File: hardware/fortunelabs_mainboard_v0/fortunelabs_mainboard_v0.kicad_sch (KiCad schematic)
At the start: 21 parts, among them J1 Conn_01x04_Pin, J4 Conn_02x08_Odd_Even, U1 ADS1115, U2 MCP23017_ML, U3 ESP32-S3-WROOM-2

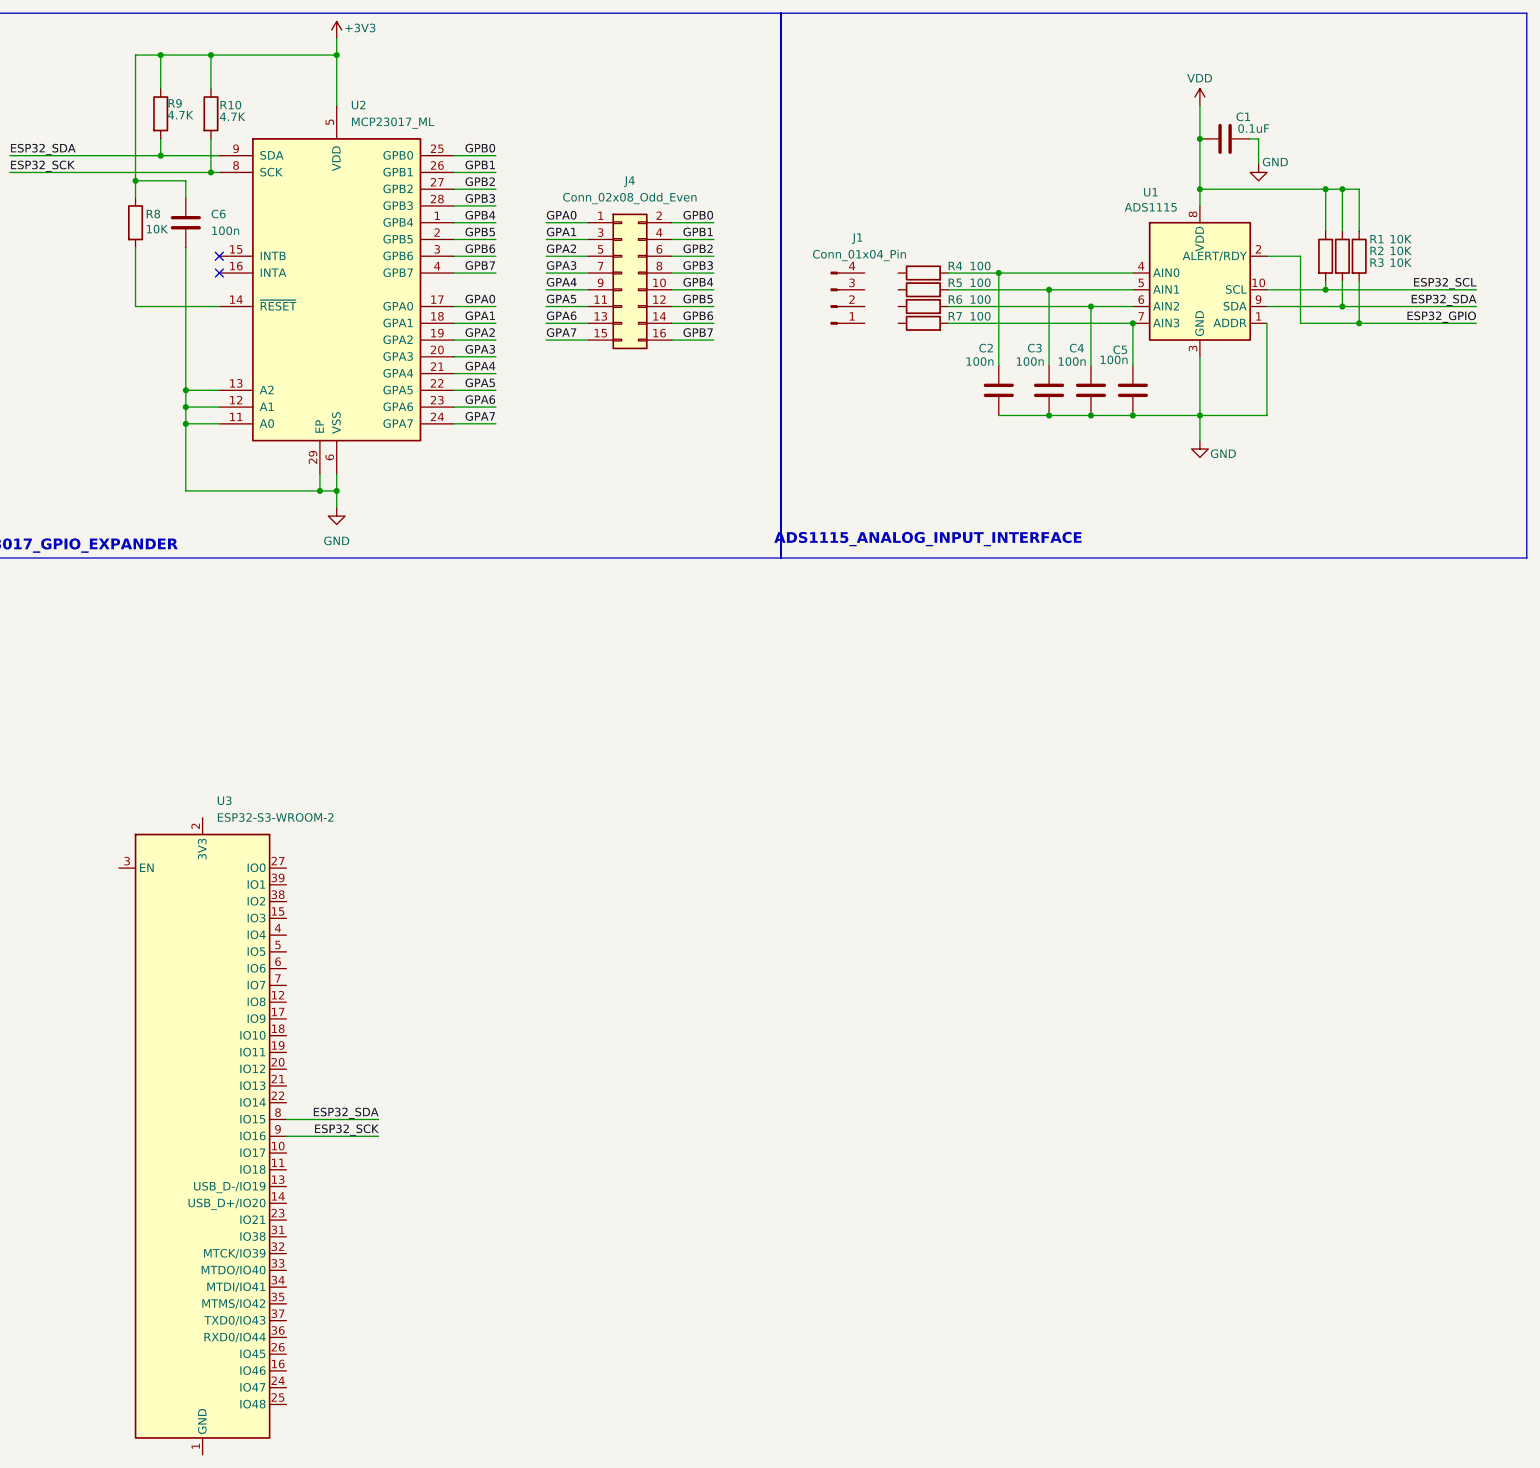
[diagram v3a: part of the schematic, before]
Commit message: refactor: changing pin to Conn_02x04_Odd_Even and restructure ground location
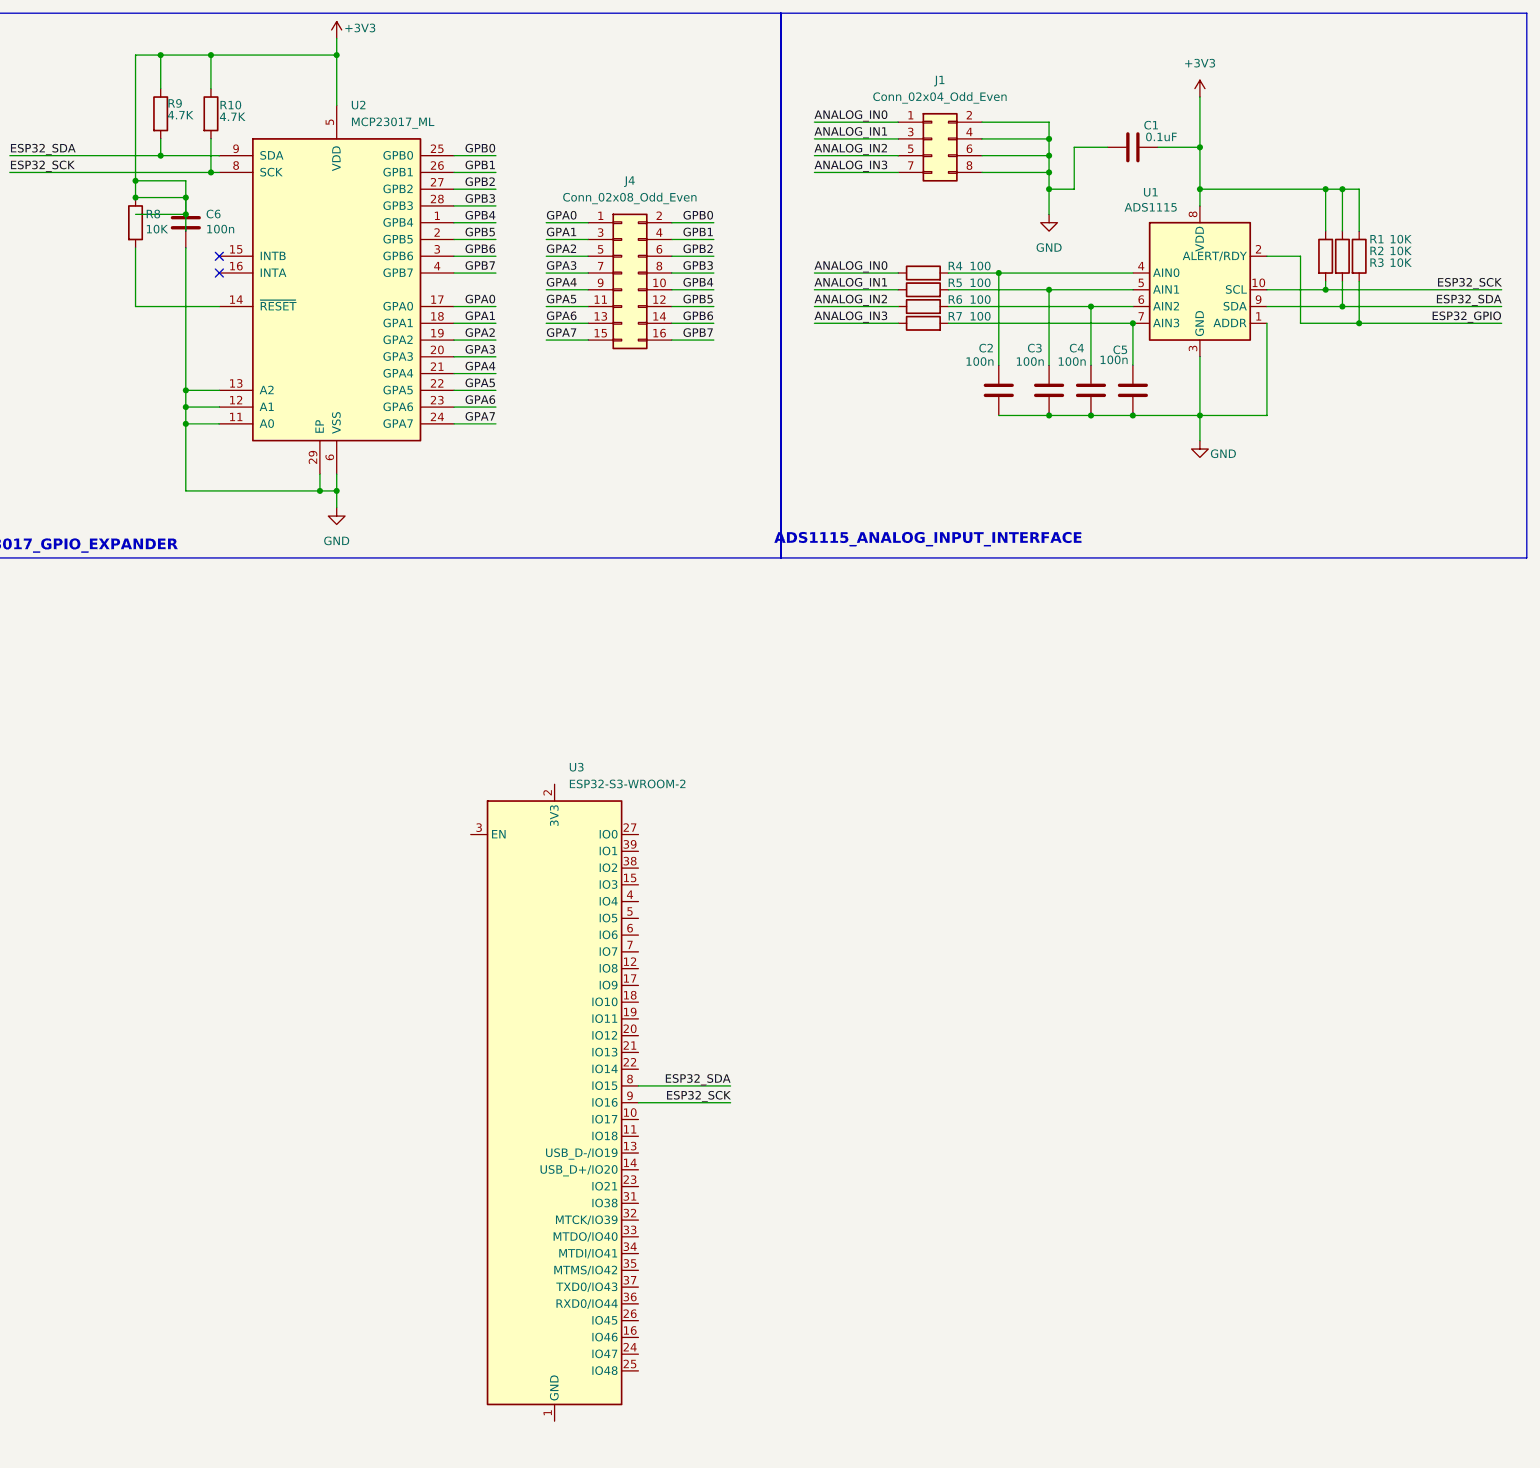
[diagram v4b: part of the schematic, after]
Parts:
- removed J1: Conn_01x04_Pin, symbol Connector:Conn_01x04_Pin
- added J1: Conn_02x04_Odd_Even, symbol Connector_Generic:Conn_02x04_Odd_Even
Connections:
- net ESP32_SCL is gone; now on net ESP32_SCK: R3.2, U1.10 (SCL)
- net +3V3: now also C1.1, R1.1, R2.1, R3.1, U1.8 (VDD)
- net GND: now also C1.2, J1.2 (Pin_2), J1.4 (Pin_4), J1.6 (Pin_6), J1.8 (Pin_8); no longer C1.1
- net ANALOG_IN2: now reaches R6.1
- net ANALOG_IN2: now also J1.5 (Pin_5)
- net ANALOG_IN0: now reaches R4.1
- net ANALOG_IN0: now also J1.1 (Pin_1)
- net ANALOG_IN1: now reaches R5.1
- net ANALOG_IN1: now also J1.3 (Pin_3)
- net ANALOG_IN3: now reaches R7.1
- net ANALOG_IN3: now also J1.7 (Pin_7)
- removed net VDD: C1.2, R1.1, R2.1, R3.1, U1.8 (VDD)
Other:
- moved on the sheet: C1, U3

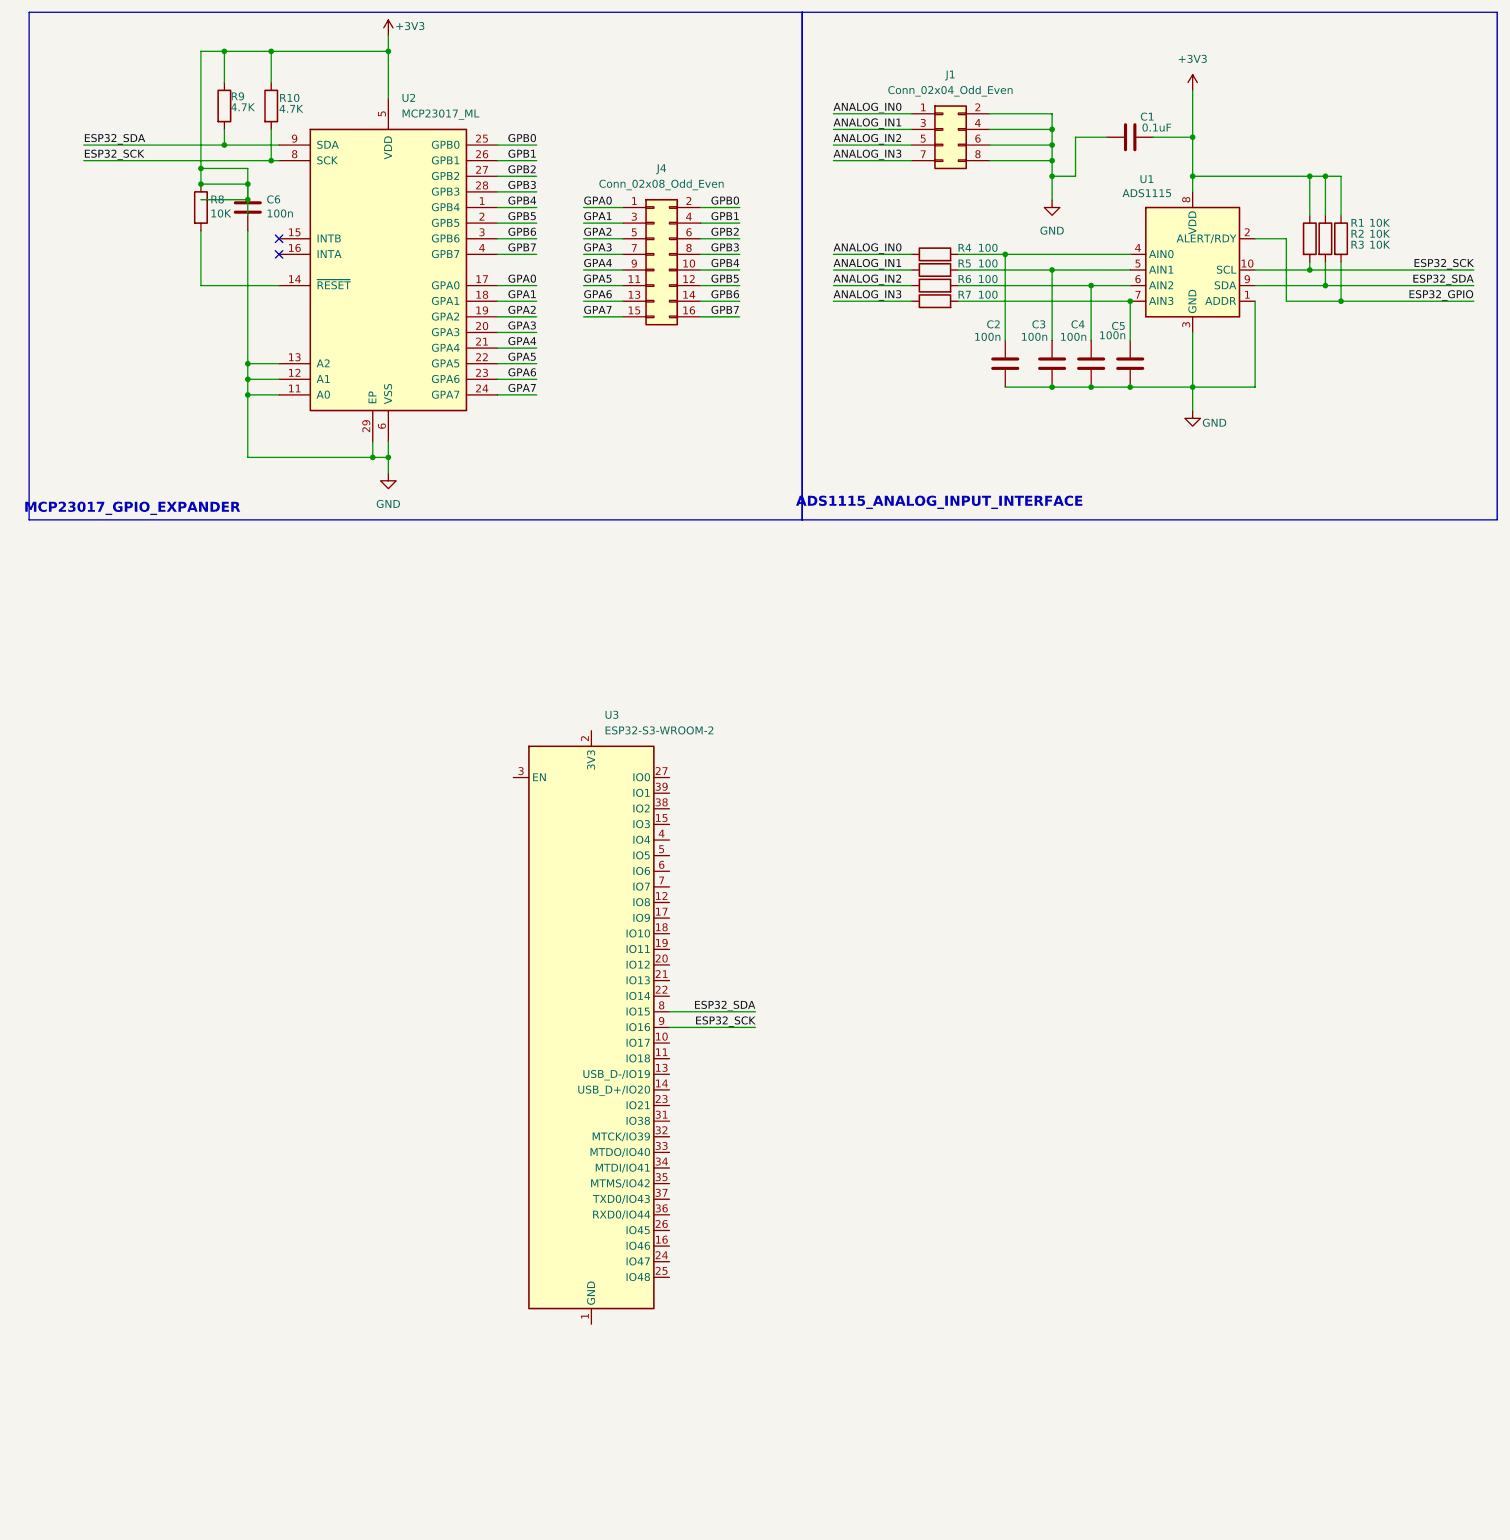
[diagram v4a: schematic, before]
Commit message: refactor: restructure i2c IO
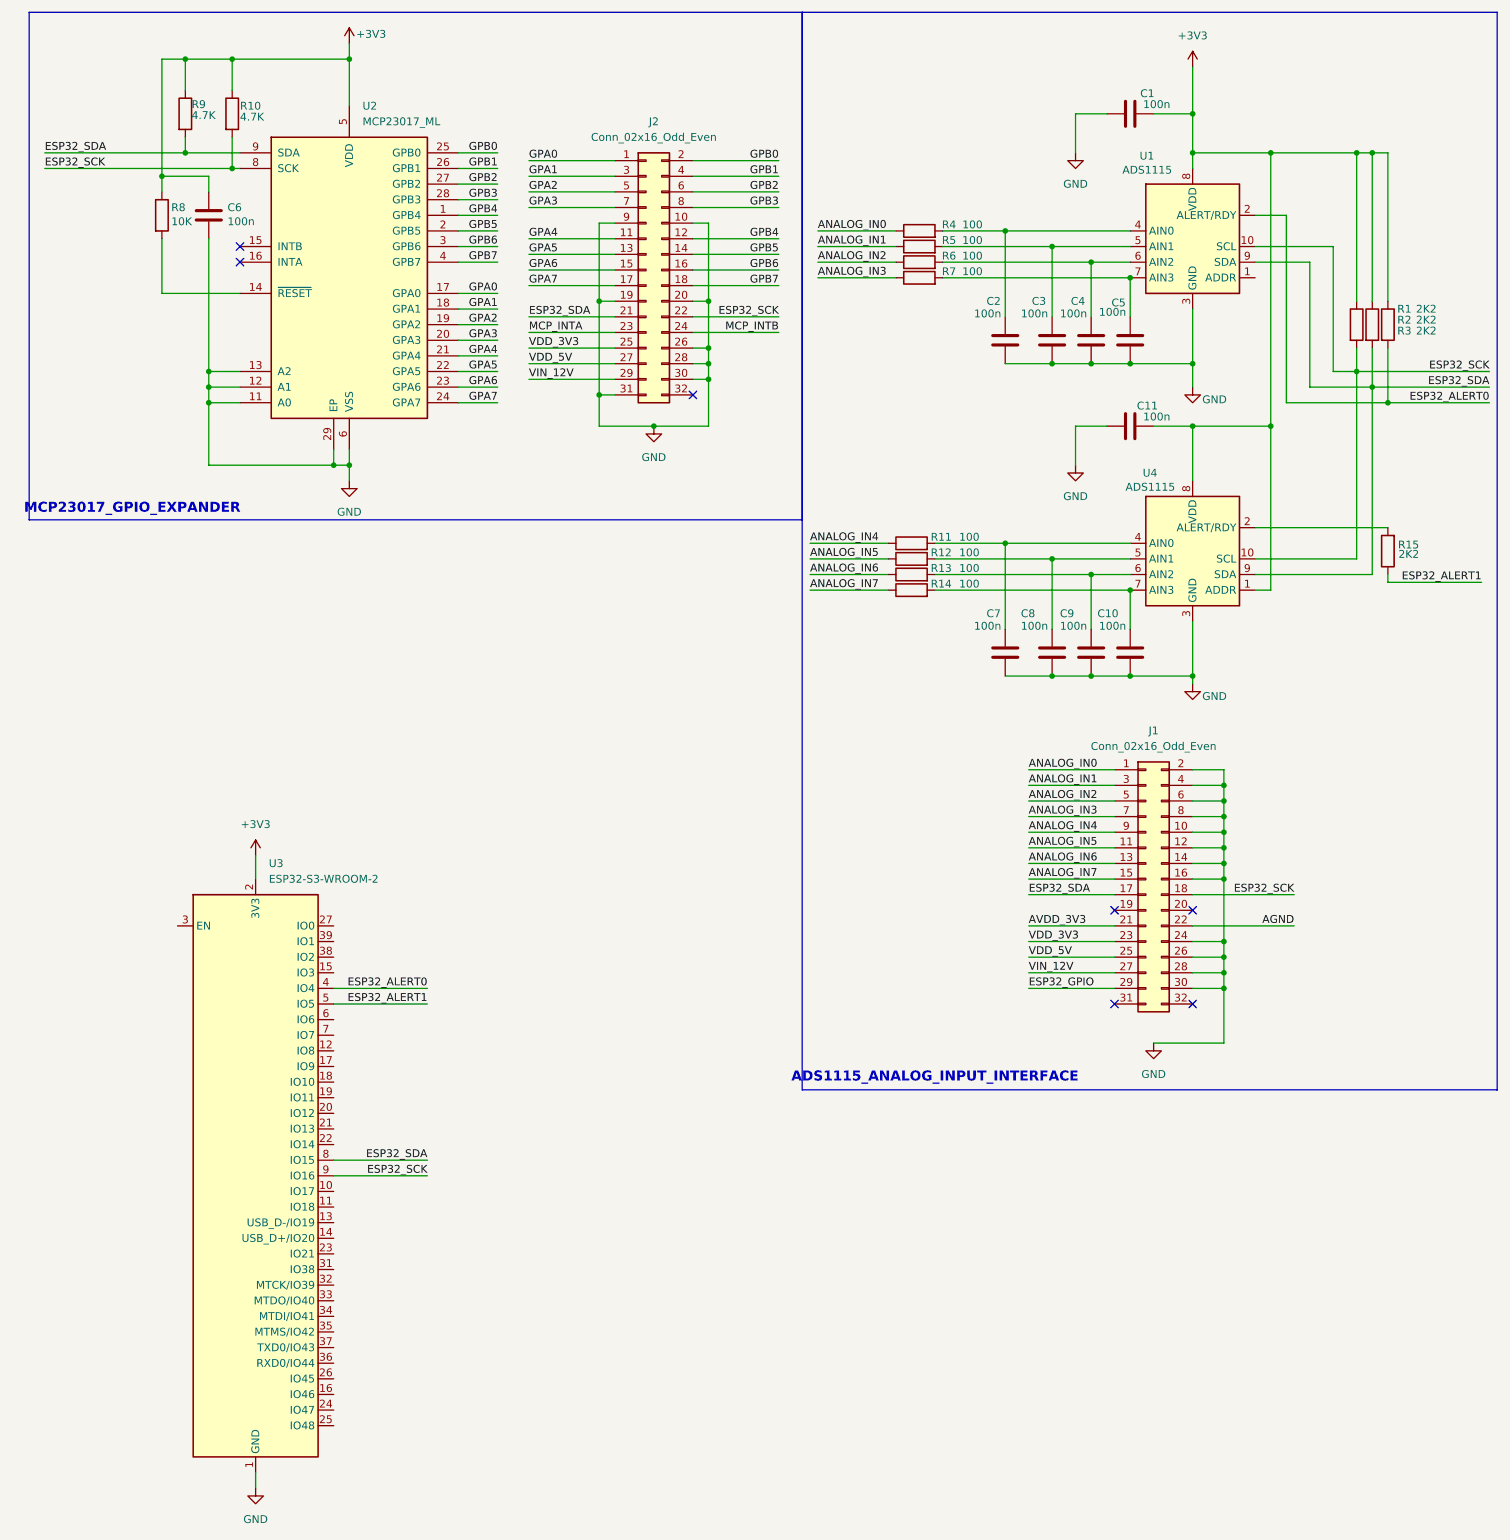
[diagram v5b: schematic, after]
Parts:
- removed J1: Conn_02x04_Odd_Even, symbol Connector_Generic:Conn_02x04_Odd_Even
- removed J4: Conn_02x08_Odd_Even, symbol Connector_Generic:Conn_02x08_Odd_Even
- added C10, C11, C7, C8, C9: 100n, symbol Device:C
- added J1, J2: Conn_02x16_Odd_Even, symbol Connector_Generic:Conn_02x16_Odd_Even
- added R11, R12, R13, R14: 100, symbol Device:R
- added R15: 2K2, symbol Device:R
- added U4: ADS1115, Package_SO:TSSOP-10_3x3mm_P0.5mm, symbol Analog_ADC:ADS1115IDGS
- C1: value 0.1uF -> 100n
- R1, R2, R3: value 10K -> 2K2
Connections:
- net +3V3: now also U3.2 (3V3), C11.1, U4.1 (ADDR), U4.8 (VDD)
- net ANALOG_IN0: now also J1.1 (Pin_1)
- net ANALOG_IN1: now also J1.3 (Pin_3)
- net ANALOG_IN2: now also J1.5 (Pin_5)
- net ANALOG_IN3: now also J1.7 (Pin_7)
- net ESP32_GPIO: now also J1.29 (Pin_29); no longer R1.2, U1.2 (ALERT/RDY)
- net ESP32_SCK: now also J1.18 (Pin_18), J2.22 (Pin_22), U4.10 (SCL)
- net ESP32_SDA: now also J1.17 (Pin_17), J2.21 (Pin_21), U4.9 (SDA)
- net GND: now also U3.1 (GND), U3.40 (GND), U3.41 (GND), C10.2, C11.2, C7.2, C8.2, C9.2, J1.10 (Pin_10), J1.12 (Pin_12), J1.14 (Pin_14), J1.16 (Pin_16), J1.2 (Pin_2), J1.24 (Pin_24), J1.26 (Pin_26), J1.28 (Pin_28), J1.30 (Pin_30), J1.4 (Pin_4), J1.6 (Pin_6), J1.8 (Pin_8), J2.10 (Pin_10), J2.19 (Pin_19), J2.20 (Pin_20), J2.26 (Pin_26), J2.28 (Pin_28), J2.30 (Pin_30), J2.31 (Pin_31), J2.9 (Pin_9), U4.3 (GND); no longer U1.1 (ADDR)
- net GPA0: now also J2.1 (Pin_1)
- net GPA1: now also J2.3 (Pin_3)
- net GPA2: now also J2.5 (Pin_5)
- net GPA3: now also J2.7 (Pin_7)
- net GPA4: now also J2.11 (Pin_11)
- net GPA5: now also J2.13 (Pin_13)
- net GPA6: now also J2.15 (Pin_15)
- net GPA7: now also J2.17 (Pin_17)
- net GPB0: now also J2.2 (Pin_2)
- net GPB1: now also J2.4 (Pin_4)
- net GPB2: now also J2.6 (Pin_6)
- net GPB3: now also J2.8 (Pin_8)
- net GPB4: now also J2.12 (Pin_12)
- net GPB5: now also J2.14 (Pin_14)
- net GPB6: now also J2.16 (Pin_16)
- net GPB7: now also J2.18 (Pin_18)
- net ESP32_ALERT0: now reaches U3.4 (IO4)
- net ESP32_ALERT0: now also R1.2, U1.2 (ALERT/RDY)
- net ESP32_ALERT1: now reaches U3.5 (IO5)
- net ESP32_ALERT1: now also R15.1
- new net: C9.1, R13.2, U4.6 (AIN2)
- new net: C8.1, R12.2, U4.5 (AIN1)
- new net: C10.1, R14.2, U4.7 (AIN3)
- new net: C7.1, R11.2, U4.4 (AIN0)
- new net: R15.2, U4.2 (ALERT/RDY)
- new net AGND: J1.22 (Pin_22)
- new net ANALOG_IN4: J1.9 (Pin_9), R11.1
- new net ANALOG_IN5: J1.11 (Pin_11), R12.1
- new net ANALOG_IN6: J1.13 (Pin_13), R13.1
- new net ANALOG_IN7: J1.15 (Pin_15), R14.1
- new net AVDD_3V3: J1.21 (Pin_21)
- new net MCP_INTA: J2.23 (Pin_23)
- new net MCP_INTB: J2.24 (Pin_24)
- new net VDD_3V3: J1.23 (Pin_23), J2.25 (Pin_25)
- new net VDD_5V: J1.25 (Pin_25), J2.27 (Pin_27)
- new net VIN_12V: J1.27 (Pin_27), J2.29 (Pin_29)
- no-connect marks 2 -> 7
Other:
- moved on the sheet: C1, C2, C3, C4, C5, C6, R1, R10, R2, R3, R4, R5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
